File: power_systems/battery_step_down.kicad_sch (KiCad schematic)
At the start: 28 parts, among them Q1 BSC520N15NS3GATMA1, Q2 BSC520N15NS3GATMA1, Q3 BSC520N15NS3GATMA1, U1 LTC7801EFE-PBF

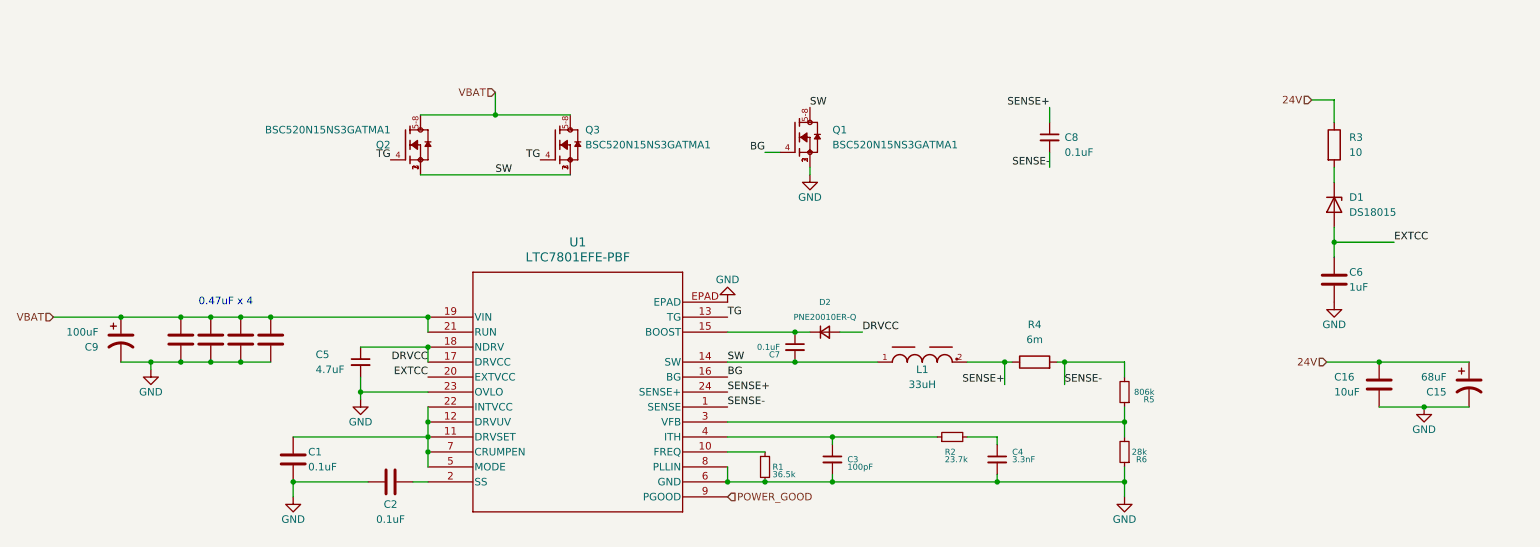
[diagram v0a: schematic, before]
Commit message: Schematics and layouting for power systems board
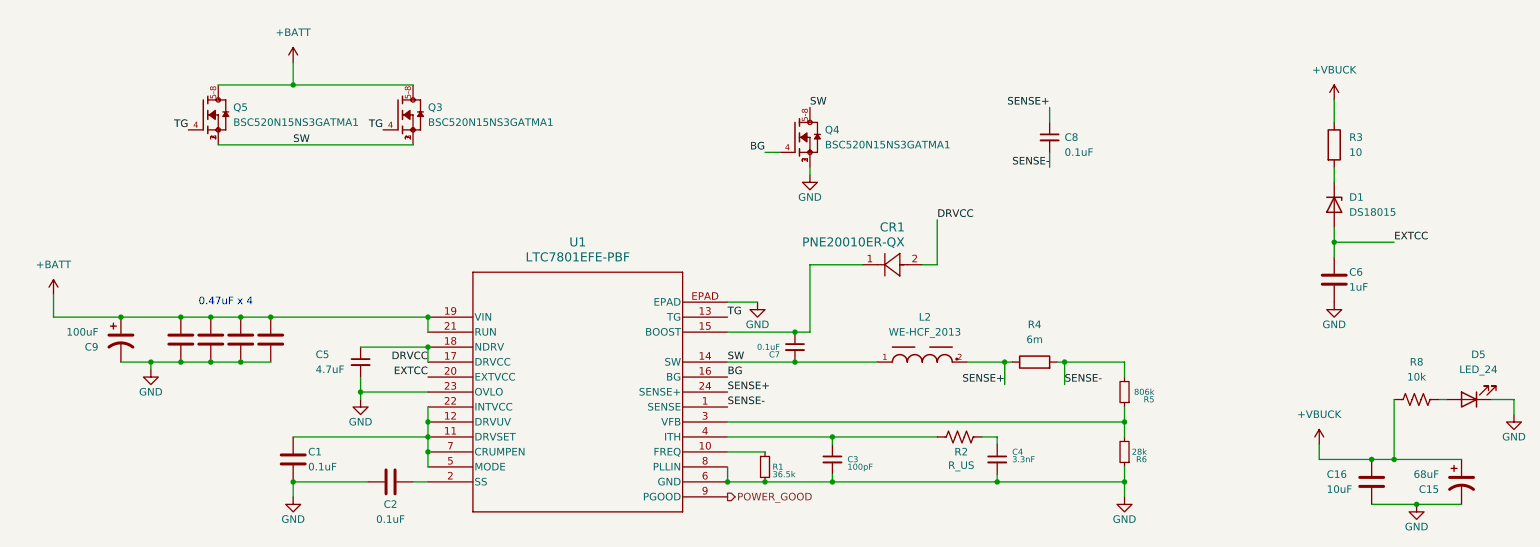
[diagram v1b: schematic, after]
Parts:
- removed D2: PNE20010ER-Q, avi_lib:CR_CFP3_SOD123W_NEX, symbol Device:D_Small
- removed L1: 33uH, avi_lib:7443633300, symbol avi_lib:WE-HCF_2013
- removed Q1, Q2, Q3: BSC520N15NS3GATMA1, avi_lib:TRANS_BSC520N15NS3GATMA1, symbol avi_lib:BSC520N15NS3GATMA1
- removed R2: 23.7k, symbol Device:R_Small
- added CR1: PNE20010ER-QX, footprints:CR_CFP3_SOD123W_NEX, symbol PNE2001:PNE20010ER-QX
- added D5: LED_24, Diode_SMD:D_0603_1608Metric, symbol Device:LED
- added L2: WE-HCF_2013, footprints:WE-HCF_2013, symbol WE-HCF_2013:WE-HCF_2013
- added Q3, Q4, Q5: BSC520N15NS3GATMA1, footprints:TRANS_BSC520N15NS3GATMA1, symbol BSC520N15NS3GATMA1:BSC520N15NS3GATMA1
- added R2: R_US, Resistor_SMD:R_0603_1608Metric, symbol Device:R_US
- added R8: 10k, Resistor_SMD:R_0603_1608Metric, symbol Device:R_US
- C1, C10, C11, C12, C13, C16, C2, C3, C4, C5, C6, C7, C8: footprint (none) -> Capacitor_SMD:C_0603_1608Metric
- C15, C9: footprint (none) -> Capacitor_SMD:CP_Elec_5x3
- D1: footprint (none) -> Diode_SMD:D_0603_1608Metric
- R1, R3, R4, R5, R6: footprint (none) -> Resistor_SMD:R_0603_1608Metric
- U1: footprint FE_24_ADI -> footprints:FE_24_ADI
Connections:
- net DRVCC: now also CR1.2
- net GND: now also D5.1 (K), Q4.1, Q4.2, Q4.3
- net SENSE+: now also L2.2
- net SW: now also L2.1, Q3.1, Q3.2, Q3.3, Q4.5-8, Q5.1, Q5.2, Q5.3
- net TG: now also Q3.4, Q5.4
- net at C7.1, U1.15 (BOOST): now also CR1.1
- net at U1.16 (BG): now also Q4.4
- net at C3.1, U1.4 (ITH): now also R2.1
- net at C4.1: now also R2.2
- net 24V renamed +VBUCK
- net +VBUCK: now also R8.1
- net VBAT renamed +BATT
- net +BATT: now also Q3.5-8, Q5.5-8
- new net: D5.2 (A), R8.2
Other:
- moved on the sheet: C15, C16

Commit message: Power systems routing v1
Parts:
- removed C15: 68uF, Capacitor_SMD:CP_Elec_5x3, symbol Device:C_Polarized_US
- removed C16: 10uF, Capacitor_SMD:C_0603_1608Metric, symbol Device:C
- removed D5: LED_24, Diode_SMD:D_0603_1608Metric, symbol Device:LED
- removed R8: 10k, Resistor_SMD:R_0603_1608Metric, symbol Device:R_US
- added C14: 10uF, Capacitor_SMD:C_0603_1608Metric, symbol Device:C
- added C17: 68uF, Capacitor_SMD:CP_Elec_5x3, symbol Device:C_Polarized_US
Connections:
- net SENSE- is gone; now on net +VBUCK: C8.2, R4.2, R5.2, U1.1 (SENSE)
- net +VBUCK: now also C14.1, C17.1
- net GND: now also C14.2, C17.2
- net POWER_GOOD: no longer names the net of U1.9 (PGOOD)
- no-connect marks 0 -> 1
